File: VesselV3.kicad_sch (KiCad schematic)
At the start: 398 parts, among them IC1 USB3320C-EZK-TR, IC3 5VOutput_VoltageRegulator, IC4 BidirectionalLogicLevelShifter, IC6 AND Gate, J1 JTAG/SWD 10pins Headers, Y1 25MHz

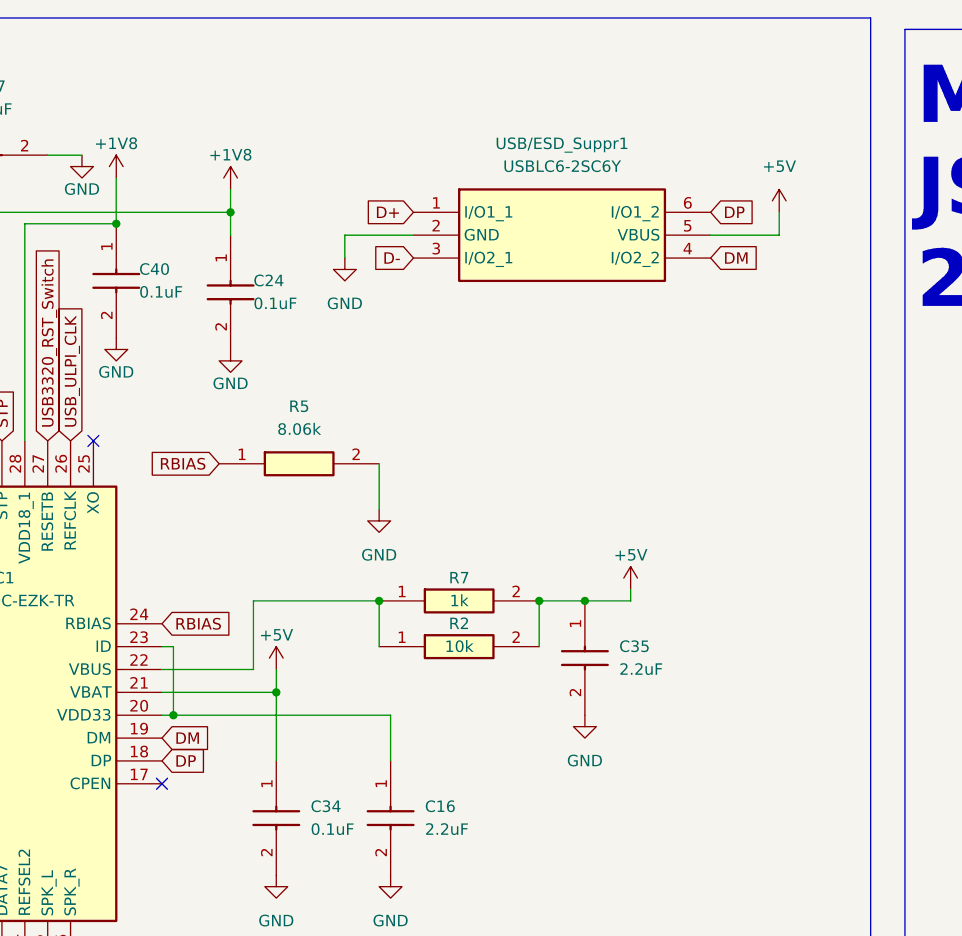
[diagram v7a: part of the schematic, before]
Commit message: USB ESD -> Internal ESD in USB3320 IC
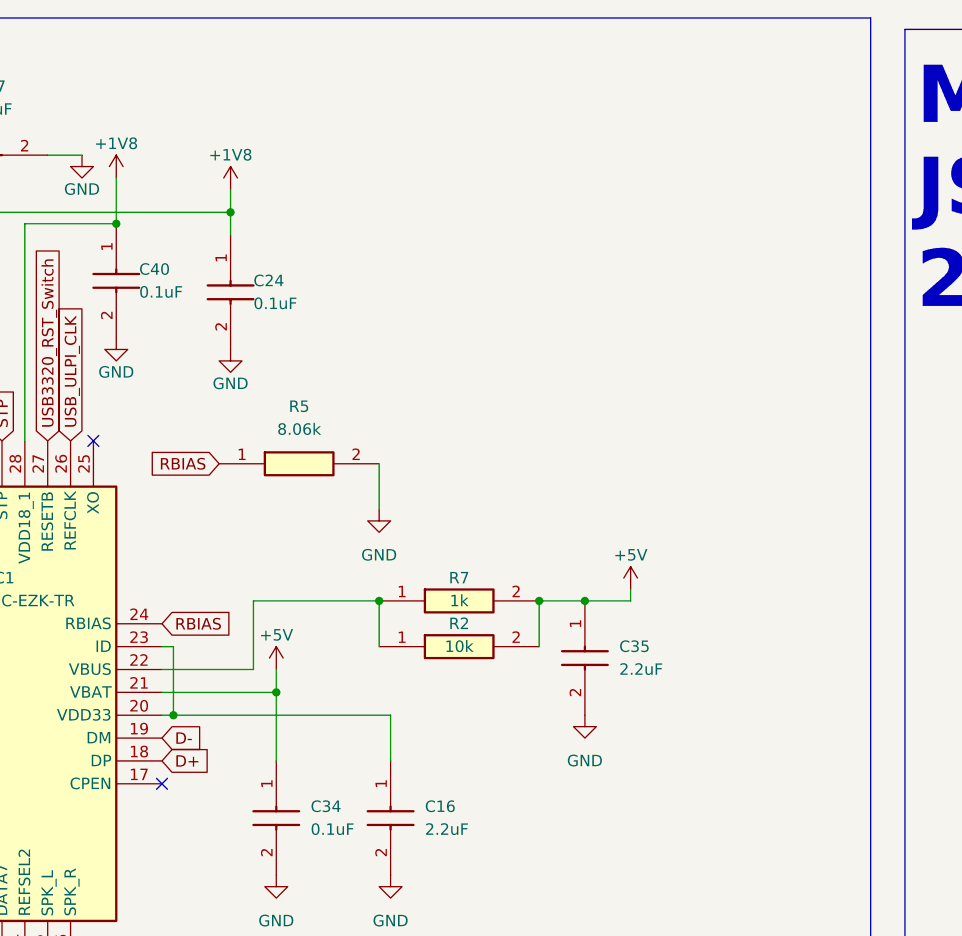
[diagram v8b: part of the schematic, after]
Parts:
- removed USB/ESD_Suppr1: USBLC6-2SC6Y, SamacSys_Parts:SOT95P280X145-6N, symbol SamacSys_Parts:USBLC6-2SC6Y
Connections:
- net DM is gone; now on net D-: IC1.19 (DM)
- net DP is gone; now on net D+: IC1.18 (DP)
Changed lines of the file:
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@@
     (stroke (width 0) (type default))
   )
-  (wire (pts (xy 491.49 34.29) (xy 491.49 36.83))
-    (stroke (width 0) (type default))
-  )
   (wire (pts (xy 273.05 394.97) (xy 270.51 394.97))
     (stroke (width 0) (type default))
@@
     (stroke (width 0) (type default))
   )
-  (wire (pts (xy 483.87 36.83) (xy 491.49 36.83))
-    (stroke (width 0) (type default))
-  )
   (wire (pts (xy 560.07 295.91) (xy 557.53 295.91))
     (stroke (width 0) (type default))
@@
     (stroke (width 0) (type default))
   )
-  (wire (pts (xy 450.85 36.83) (xy 443.23 36.83))
-    (stroke (width 0) (type default))
-  )
   (wire (pts (xy 737.87 328.93) (xy 788.67 328.93))
     (stroke (width 0) (type default))
@@
     (stroke (width 0) (type default))
   )
-  (wire (pts (xy 443.23 36.83) (xy 443.23 39.37))
-    (stroke (width 0) (type default))
-  )
   (wire (pts (xy 71.12 185.42) (xy 111.76 185.42))
     (stroke (width 0) (type default))
@@
     )
   )
-  (global_label "DM" (shape input) (at 422.91 92.71 0) (fields_autoplaced)
-    (effects (font (size 1.27 1.27)) (justify left))
-    (property "Intersheetrefs" "${INTERSHEET_REFS}" (at 428.6166 92.71 0)
-      (effects (font (size 1.27 1.27)) (justify left) hide)
-    )
-  )
   (global_label "COL5" (shape input) (at 633.73 54.61 90) (fields_autoplaced)
     (effects (font (size 1.27 1.27)) (justify left))
@@
     )
   )
-  (global_label "DM" (shape input) (at 483.87 39.37 0) (fields_autoplaced)
-    (effects (font (size 1.27 1.27)) (justify left))
-    (property "Intersheetrefs" "${INTERSHEET_REFS}" (at 489.5766 39.37 0)
-      (effects (font (size 1.27 1.27)) (justify left) hide)
-    )
-  )
   (global_label "ROW3" (shape input) (at 36.83 121.92 180) (fields_autoplaced)
     (effects (font (size 1.27 1.27)) (justify right))
@@
     )
   )
-  (global_label "D+" (shape input) (at 450.85 34.29 180) (fields_autoplaced)
-    (effects (font (size 1.27 1.27)) (justify right))
-    (property "Intersheetrefs" "${INTERSHEET_REFS}" (at 445.0224 34.29 0)
-      (effects (font (size 1.27 1.27)) (justify right) hide)
+  (global_label "D+" (shape input) (at 422.91 95.25 0) (fields_autoplaced)
+    (effects (font (size 1.27 1.27)) (justify left))
+    (property "Intersheetrefs" "${INTERSHEET_REFS}" (at 428.7376 95.25 0)
+      (effects (font (size 1.27 1.27)) (justify left) hide)
     )
   )
@@
     )
   )
-  (global_label "DP" (shape input) (at 483.87 34.29 0) (fields_autoplaced)
-    (effects (font (size 1.27 1.27)) (justify left))
-    (property "Intersheetrefs" "${INTERSHEET_REFS}" (at 489.3952 34.29 0)
-      (effects (font (size 1.27 1.27)) (justify left) hide)
-    )
-  )
   (global_label "BOOT0_PIN" (shape input) (at 638.81 54.61 90) (fields_autoplaced)
     (effects (font (size 1.27 1.27)) (justify left))
@@
     )
   )
-  (global_label "D-" (shape input) (at 450.85 39.37 180) (fields_autoplaced)
-    (effects (font (size 1.27 1.27)) (justify right))
-    (property "Intersheetrefs" "${INTERSHEET_REFS}" (at 445.0224 39.37 0)
-      (effects (font (size 1.27 1.27)) (justify right) hide)
+  (global_label "D-" (shape input) (at 422.91 92.71 0) (fields_autoplaced)
+    (effects (font (size 1.27 1.27)) (justify left))
+    (property "Intersheetrefs" "${INTERSHEET_REFS}" (at 428.7376 92.71 0)
+      (effects (font (size 1.27 1.27)) (justify left) hide)
     )
   )
@@
     )
   )
-  (global_label "DP" (shape input) (at 422.91 95.25 0) (fields_autoplaced)
-    (effects (font (size 1.27 1.27)) (justify left))
-    (property "Intersheetrefs" "${INTERSHEET_REFS}" (at 428.4352 95.25 0)
-      (effects (font (size 1.27 1.27)) (justify left) hide)
-    )
-  )
   (global_label "COL7" (shape input) (at 124.46 30.48 90) (fields_autoplaced)
     (effects (font (size 1.27 1.27)) (justify left))
@@
     )
   )
-  (symbol (lib_id "SamacSys_Parts:USBLC6-2SC6Y") (at 450.85 34.29 0) (unit 1)
-    (in_bom yes) (on_board yes) (dnp no) (fields_autoplaced)
-    (property "Reference" "USB/ESD_Suppr1" (at 467.36 26.67 0)
-      (effects (font (size 1.27 1.27)))
-    )
-    (property "Value" "USBLC6-2SC6Y" (at 467.36 29.21 0)
-      (effects (font (size 1.27 1.27)))
-    )
-    (property "Footprint" "SamacSys_Parts:SOT95P280X145-6N" (at 480.06 129.21 0)
-      (effects (font (size 1.27 1.27)) (justify left top) hide)
-    )
-    (property "Datasheet" "https://componentsearchengine.com/Datasheets/1/USBLC6-2SC6Y.pdf" (at 480.06 229.21 0)
-      (effects (font (size 1.27 1.27)) (justify left top) hide)
-    )
-    (property "Height" "1.45" (at 480.06 429.21 0)
-      (effects (font (size 1.27 1.27)) (justify left top) hide)
-    )
-    (property "Mouser Part Number" "511-USBLC6-2SC6Y" (at 480.06 529.21 0)
-      (effects (font (size 1.27 1.27)) (justify left top) hide)
-    )
-    (property "Mouser Price/Stock" "https://www.mouser.co.uk/ProductDetail/STMicroelectronics/USBLC6-2SC6Y?qs=gNDSiZmRJS%2FOgDexvXkdow%3D%3D" (at 480.06 629.21 0)
-      (effects (font (size 1.27 1.27)) (justify left top) hide)
-    )
-    (property "Manufacturer_Name" "STMicroelectronics" (at 480.06 729.21 0)
-      (effects (font (size 1.27 1.27)) (justify left top) hide)
-    )
-    (property "Manufacturer_Part_Number" "USBLC6-2SC6Y" (at 480.06 829.21 0)
-      (effects (font (size 1.27 1.27)) (justify left top) hide)
-    )
-    (property "DigikeyPartNumber" "497-11882-2-ND" (at 450.85 34.29 0)
-      (effects (font (size 1.27 1.27)) hide)
-    )
-    (property "Sim.Library" "C:\\Users\\Ismael\\Desktop\\Perso Projects\\5 - IBS_Spice Models\\en.usblc6-2sc6y_pspice\\USBLC6-2SC6Y.lib" (at 450.85 34.29 0)
-      (effects (font (size 1.27 1.27)) hide)
-    )
-    (property "Sim.Name" "USBLC6-2SC6Y" (at 450.85 34.29 0)
-      (effects (font (size 1.27 1.27)) hide)
-    )
-    (property "Sim.Device" "SUBCKT" (at 450.85 34.29 0)
-      (effects (font (size 1.27 1.27)) hide)
-    )
-    (property "Sim.Pins" "1=1 2=2 3=3 4=4 5=5 6=6" (at 450.85 34.29 0)
-      (effects (font (size 1.27 1.27)) hide)
-    )
-    (pin "1")
-    (pin "2")
-    (pin "3")
-    (pin "4")
-    (pin "5")
-    (pin "6")
-    (instances
-      (project "VesselV3"
-        (path "/7364f6a3-b999-47c8-8f6d-f83e5421d1ed"
-          (reference "USB/ESD_Suppr1") (unit 1)
-        )
-      )
-    )
-  )
   (symbol (lib_id "WS2812BNano4684RGB-3rdParty:4684") (at 36.83 394.97 0) (unit 1)
     (in_bom yes) (on_board yes) (dnp no)
@@
     )
   )
-  (symbol (lib_id "power:GND") (at 443.23 39.37 0) (unit 1)
-    (in_bom yes) (on_board yes) (dnp no) (fields_autoplaced)
-    (property "Reference" "#PWR019" (at 443.23 45.72 0)
-      (effects (font (size 1.27 1.27)) hide)
-    )
-    (property "Value" "GND" (at 443.23 44.45 0)
-      (effects (font (size 1.27 1.27)))
-    )
-    (property "Footprint" "" (at 443.23 39.37 0)
-      (effects (font (size 1.27 1.27)) hide)
-    )
-    (property "Datasheet" "" (at 443.23 39.37 0)
-      (effects (font (size 1.27 1.27)) hide)
-    )
-    (pin "1")
-    (instances
-      (project "VesselV3"
-        (path "/7364f6a3-b999-47c8-8f6d-f83e5421d1ed"
-          (reference "#PWR019") (unit 1)
-        )
-      )
-    )
-  )
   (symbol (lib_id "power:GND") (at 364.49 199.39 0) (unit 1)
     (in_bom yes) (on_board yes) (dnp no)
@@
         )
       )
-    )
-  )
-  (symbol (lib_id "power:+5V") (at 491.49 34.29 0) (unit 1)
-    (in_bom yes) (on_board yes) (dnp no) (fields_autoplaced)
-    (property "Reference" "#PWR063" (at 491.49 38.1 0)
-      (effects (font (size 1.27 1.27)) hide)
-    )
-    (property "Value" "+5V" (at 491.49 29.21 0)
-      (effects (font (size 1.27 1.27)))
-    )
-    (property "Footprint" "" (at 491.49 34.29 0)
-      (effects (font (size 1.27 1.27)) hide)
-    )
-    (property "Datasheet" "" (at 491.49 34.29 0)
-      (effects (font (size 1.27 1.27)) hide)
-    )
-    (pin "1")
-    (instances
-      (project "VesselV3"
-        (path "/7364f6a3-b999-47c8-8f6d-f83e5421d1ed"
-          (reference "#PWR063") (unit 1)
-        )
-      )
